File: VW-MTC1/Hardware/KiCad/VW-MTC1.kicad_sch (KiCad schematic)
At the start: 7 parts

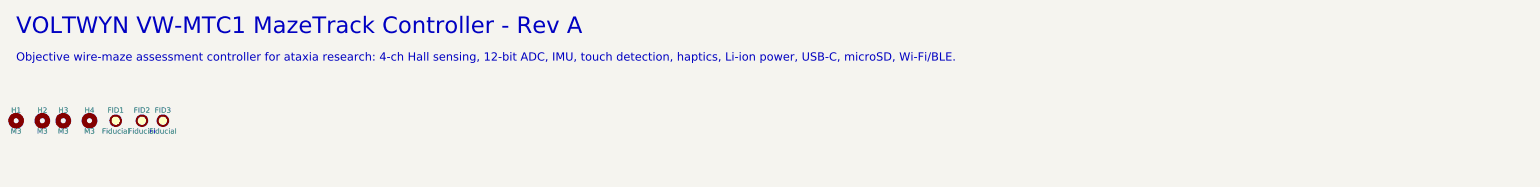
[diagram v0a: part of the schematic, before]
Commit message: Apply Rev B touch circuit, routed PCB and topology-tested BOM
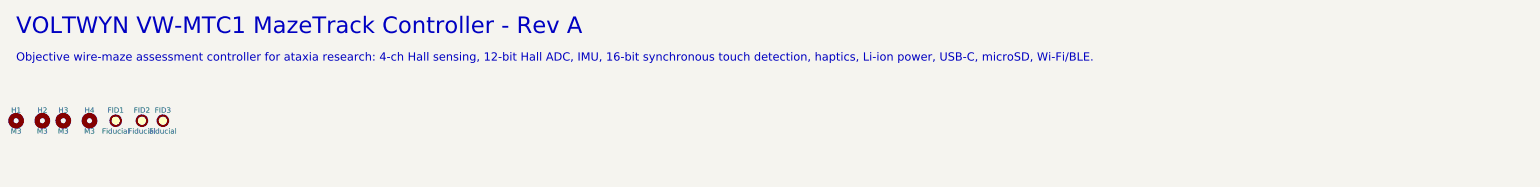
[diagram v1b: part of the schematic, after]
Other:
- note added: "Objective wire-maze assessment controller for ataxia research: 4-ch Hall sensing, 12-bit Hall ADC, IMU, 16-bit synchronous touch detection, haptics, Li-ion power, USB-C, microSD, Wi-Fi/BLE."
- note removed: "Objective wire-maze assessment controller for ataxia research: 4-ch Hall sensing, 12-bit ADC, IMU, touch detection, haptics, Li-ion power, USB-C, microSD, Wi-Fi/BLE."
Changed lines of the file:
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@@
 	(title_block
 		(title "VW-MTC1 MazeTrack Controller - Top level")
-		(date "2026-10-19")
-		(rev "A")
+		(date "2026-10-21")
+		(rev "B")
 		(company "Voltwyn")
 		(comment 1 "VW-MTC1 MazeTrack Controller - Root")
@@
 		)
 	)
-	(text "Objective wire-maze assessment controller for ataxia research: 4-ch Hall sensing, 12-bit ADC, IMU, touch detection, haptics, Li-ion power, USB-C, microSD, Wi-Fi/BLE."
+	(text "Objective wire-maze assessment controller for ataxia research: 4-ch Hall sensing, 12-bit Hall ADC, IMU, 16-bit synchronous touch detection, haptics, Li-ion power, USB-C, microSD, Wi-Fi/BLE."
 		(exclude_from_sim no)
 		(at 25.4 27.94 0)
